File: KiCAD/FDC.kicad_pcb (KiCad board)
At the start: 2 copper layers, 72.6 x 65.5 mm, 26 parts, among them J2 Conn_02x20_Odd_Even, J3 SD_Card, Q1 SSM3K324RLFCT-ND, Q2 SSM3K324RLFCT-ND, U1 SN74LVCC4245ADWR, U2 Pico, U3 SN74LVCC4245ADWR, U4 SN74LVCC4245ADWR, U5 SN74LVCC4245ADWR

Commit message: First upload of test board.
First upload of test board.
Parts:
- removed the C4 at (182.7, 80.7)
- removed C5, C6, C7, C8: 100nF, Capacitor_SMD:C_0805_2012Metric_Pad1.18x1.45mm_HandSolder
- removed D2: PMEG4010CEJ, Diode_SMD:D_SOD-323F
- removed J2: Conn_02x20_Odd_Even, Connector_PinSocket_2.54mm:PinSocket_2x20_P2.54mm_Vertical
- removed J3: SD_Card, Connector_Card:SD_Kyocera_145638009511859+
- removed the R2 at (137.7, 79.6)
- removed U4, U5: SN74LVCC4245ADWR, Package_SO:SOIC-24W_7.5x15.4mm_P1.27mm
- added J1: Conn_01x04, Connector_PinHeader_2.54mm:PinHeader_1x04_P2.54mm_Vertical, F.Cu at (142.3, 70.7)
- added R1: 1k, Resistor_SMD:R_0805_2012Metric_Pad1.20x1.40mm_HandSolder, F.Cu at (137.5, 49.0)
- added SDCARD1: ST-TF-003A, 00-ProjectLib:MicroSD_Card_TB, F.Cu at (145.7, 38.8)
- added U2: 74HCT245, Package_SO:SOIC-20W_7.5x15.4mm_P1.27mm, F.Cu at (143.1, 107.0)
- added U6: Z80, Package_DIP:DIP-40_W15.24mm, F.Cu at (116.5, 87.9)
- added U7: Z80, Package_DIP:DIP-40_W15.24mm, F.Cu at (113.0, 87.9)
- C4: renamed from C9; moved to F.Cu
- D1: footprint LED_SMD:LED_2816_7142Metric_Pad3.20x4.45mm_HandSolder -> LED_THT:LED_D5.0mm
- PICO2: renamed from U2; value Pico -> Pico 2; footprint MCU_RaspberryPi_and_Boards:RPi_Pico_SMD_TH -> Module:RaspberryPi_Pico_SMD
- Q1, Q2: value SSM3K324RLFCT-ND -> 2N7002
- R2: renamed from R3; moved to F.Cu
- R3: renamed from R4; moved to F.Cu
- U1, U3: value SN74LVCC4245ADWR -> 74HCT245; footprint Package_SO:SOIC-24W_7.5x15.4mm_P1.27mm -> Package_SO:SOIC-20W_7.5x15.4mm_P1.27mm
- moved R5 83.7 mm to (122.0, 121.5), turned to 0 degrees
- moved Q2 82.9 mm to (122.5, 118.3), turned to 180 degrees
- moved D1 69.9 mm to (144.0, 51.0)
- moved R4 69.9 mm to (123.8, 128.5), turned to 180 degrees
- moved Q1 66.3 mm to (123.0, 125.5), turned to 0 degrees
- moved R6 63.1 mm to (140.8, 52.0)
- moved U1 56.4 mm to (143.1, 127.0), turned to 0 degrees
- moved C3 53.3 mm to (150.6, 117.5), turned to 0 degrees
- moved R3 52.5 mm to (143.0, 42.5), turned to -90 degrees
- moved R2 48.4 mm to (152.0, 42.5), turned to 90 degrees
- moved C4 47.3 mm to (147.0, 42.5), turned to -90 degrees
- moved PICO2 47.3 mm to (123.2, 50.0), turned to 0 degrees
- moved C2 29.9 mm to (151.1, 97.5), turned to 0 degrees
- moved C1 15.7 mm to (150.6, 77.0), turned to 0 degrees
- moved U3 14.7 mm to (143.0, 86.5), turned to 0 degrees
- renumbered R6 to R4, R8 to R5, R1 to R6
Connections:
- C1 pad 1: +3V3 -> +5V
- C2 pad 1: +3V3 -> +5V
- PICO2 pad 15: /RD' -> /RD*
- PICO2 pad 16: /WR' -> /WR*
- R2 pad 1: Net-(J3-DAT1) -> +3V3
- R2 pad 2: +3V3 -> Net-(SDCARD1-DAT1)
- U1 pad 1: +5V -> /DIR
- U1 pad 10: /IN* -> GND
- U1 pad 11: GND -> /D4'
- U1 pad 12: GND -> /D7'
- U1 pad 13: GND -> /D1'
- U1 pad 14: /IN' -> /D6'
- U1 pad 15: /RD' -> /D3'
- U1 pad 16: /WR' -> /D5'
- U1 pad 17: /OUT' -> /D0'
- U1 pad 18: /MREQ' -> /D2'
- U1 pad 19: unconnected-(U1-B3-Pad19) -> /DATAB_OE
- U1 pad 2: +5V -> /D2
- U1 pad 20: unconnected-(U1-B2-Pad20) -> +5V
- U1 pad 3: /SYSRES* -> /D0
- U1 pad 4: unconnected-(U1-A2-Pad4) -> /D5
- U1 pad 5: unconnected-(U1-A3-Pad5) -> /D3
- U1 pad 6: /RAS* -> /D6
- U1 pad 7: /OUT* -> /D1
- U1 pad 8: /WR* -> /D7
- U1 pad 9: /RD* -> /D4
- U3 pad 10: /D2 -> GND
- U3 pad 11: GND -> /D0'
- U3 pad 12: GND -> /D1'
- U3 pad 13: GND -> /D2'
- U3 pad 14: /D2' -> /D3'
- U3 pad 15: /D0' -> /D7'
- U3 pad 16: /D5' -> /D6'
- U3 pad 17: /D3' -> /D5'
- U3 pad 18: /D6' -> /D4'
- U3 pad 19: /D1' -> /ADDRH_OE
- U3 pad 2: /DIR -> /A12
- U3 pad 20: /D7' -> +5V
- U3 pad 3: /D4 -> /A13
- U3 pad 4: /D7 -> /A14
- U3 pad 5: /D1 -> /A15
- U3 pad 6: /D6 -> /A11
- U3 pad 7: /D3 -> /A10
- U3 pad 8: /D5 -> /A9
- U3 pad 9: /D0 -> /A8
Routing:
- net GND: track 446.6 -> 40.2 mm, vias 6 -> 388
- net +3V3: track 199.1 -> 35.8 mm, vias 10 -> 0
- net /RD*: track 5.17 -> 96.1 mm, vias 0 -> 1
- net /WR*: track 4.64 -> 92.3 mm, vias 0 -> 1
- net /DATAB_OE: track 28.3 -> 109.0 mm, vias 0 -> 2
- net +5V: track 122.9 -> 197.1 mm, vias 9 -> 3
- net /DIR: track 22.7 -> 87.8 mm
- net /WAIT': track 44.5 -> 100.5 mm
- net /D4: track 12.1 -> 54.2 mm, vias 0 -> 1
- net /ADDRL_OE: track 33.4 -> 73.1 mm, vias 0 -> 4
- net /D6: track 10.6 -> 45.7 mm, vias 1 -> 0
- net /D3: track 11.0 -> 45.9 mm, vias 0 -> 1
- net /A11: track 16.4 -> 50.1 mm, vias 0 -> 1
- net /D5: track 10.5 -> 40.7 mm, vias 0 -> 1
- net /D7: track 11.6 -> 41.7 mm, vias 0 -> 1
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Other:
- board size 72.6 x 65.5 mm -> 47 x 115.5 mm
- board text added: "IN"
- board text added: "OUT"
- board text added: "Pico2"
- board text added: "Q1,Q2 - 2N7002 R1,R2,R3,R4,R5 - 1k C1,C2,C3,C4 - 100NF R6 - 100 OHM U1,U2,U3 - 74HCT245"
- board text added: "RAS"
- board text added: "SYSRES"
- board text added: "Z80"

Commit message: New PCB.. this may fit
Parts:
- PICO2: moved to B.Cu
- moved Q1 79.2 mm to (144.7, 49.4), turned to 180 degrees
- moved Q2 79.0 mm to (144.8, 42.5)
- moved R5 78.2 mm to (142.3, 46.0), turned to 180 degrees
- moved R4 78.1 mm to (142.3, 52.7)
- moved SDCARD1 32.1 mm to (163.7, 65.3), turned to -90 degrees
- moved R2 24.3 mm to (158.0, 66.0), turned to 0 degrees
- moved PICO2 22.8 mm to (140.3, 65.0), turned to 180 degrees
- moved C4 22.7 mm to (158.0, 62.3), turned to 180 degrees
- moved R3 22.2 mm to (158.0, 58.8), turned to 180 degrees
- moved U6 18.5 mm to (132.3, 97.5)
- moved U7 18.5 mm to (128.8, 97.5)
- moved D1 17.6 mm to (161.4, 48.4), turned to 180 degrees
- moved R1 15.4 mm to (134.3, 64.0)
- moved R6 13.9 mm to (154.6, 52.5), turned to -90 degrees
- moved U1 13.8 mm to (156.3, 131.1)
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- renumbered C3 to C1, C1 to C3
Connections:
- J1 pad 1: /IN' -> /SYSRES'
- J1 pad 2: /OUT' -> /IN'
- J1 pad 3: /MREQ' -> /OUT'
- J1 pad 4: /SYSRES' -> /MREQ'
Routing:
- net /WAIT*: track 10.1 -> 109.6 mm
- net /WAIT': track 100.5 -> 8.54 mm, vias 0 -> 1
- net /INT': track 97.9 -> 8.64 mm, vias 0 -> 1
- net /INT*: track 20.4 -> 105.2 mm, vias 2 -> 0
- net /DIR: track 87.8 -> 128.6 mm, vias 0 -> 3
- net /DATAB_OE: track 109.0 -> 70.1 mm, vias 2 -> 1
- net /D4': track 88.8 -> 126.0 mm, vias 5 -> 4
- net /ADDRH_OE: track 56.1 -> 19.3 mm, vias 2 -> 1
- net /OUT': track 41.0 -> 8.38 mm, vias 1 -> 0
- net /D1': track 72.9 -> 102.2 mm
- net /IN': track 34.1 -> 6.18 mm, vias 1 -> 0
- net /MREQ': track 38.8 -> 10.9 mm, vias 2 -> 0
- net /D6': track 95.5 -> 122.4 mm
- net /ADDRL_OE: track 73.1 -> 47.4 mm, vias 4 -> 1
- net /A8: track 11.1 -> 36.8 mm
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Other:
- board size 47 x 115.5 mm -> 53.5 x 110.5 mm
- board text added: "74HCT245"
- board text added: "<--Pin1"
- board text added: "Floppy80-M1 Internal version by dabone 2026 https://github.com/dabonetn/Floppy80-M1-Internal"
- board text added: "Socket-> Pins<-"
- board text removed: "Pico2"

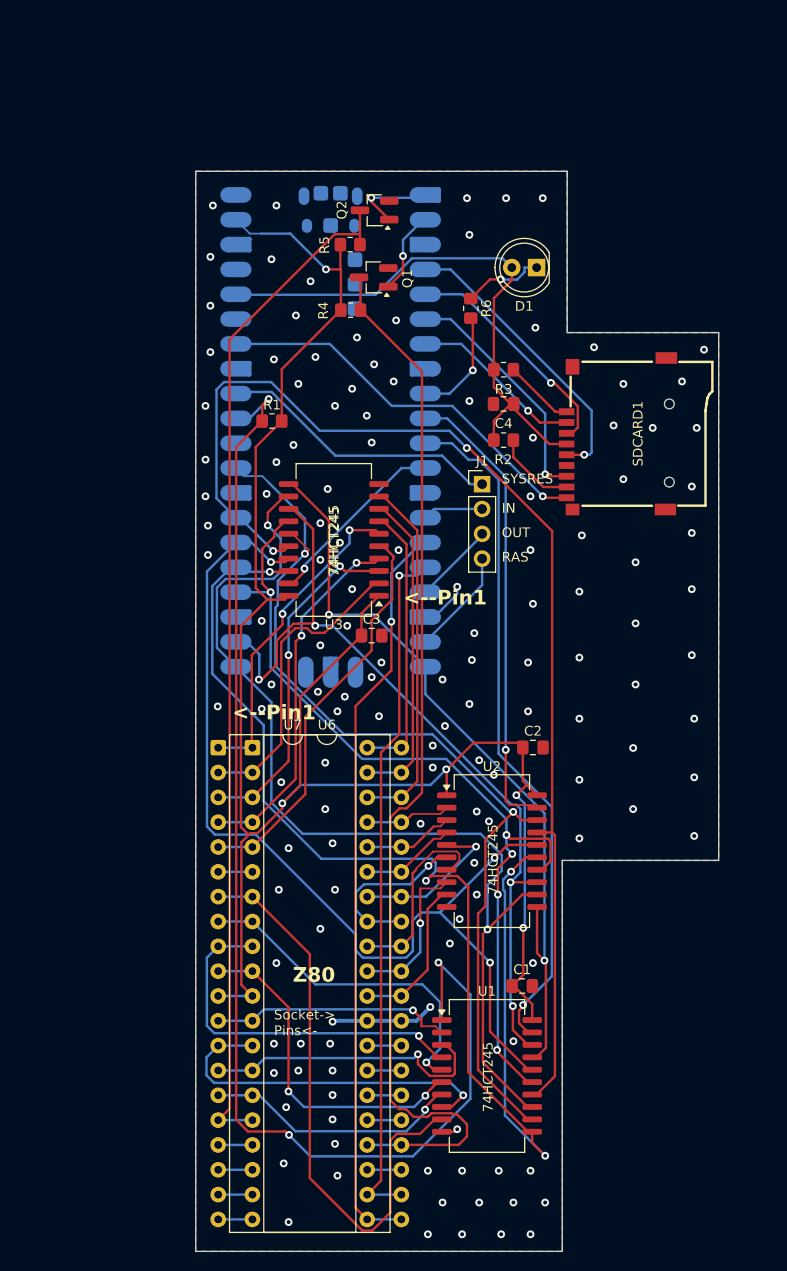
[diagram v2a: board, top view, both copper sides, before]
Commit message: Updated PCB to ver 1.01
I didn't account for some signals on the first pcb.
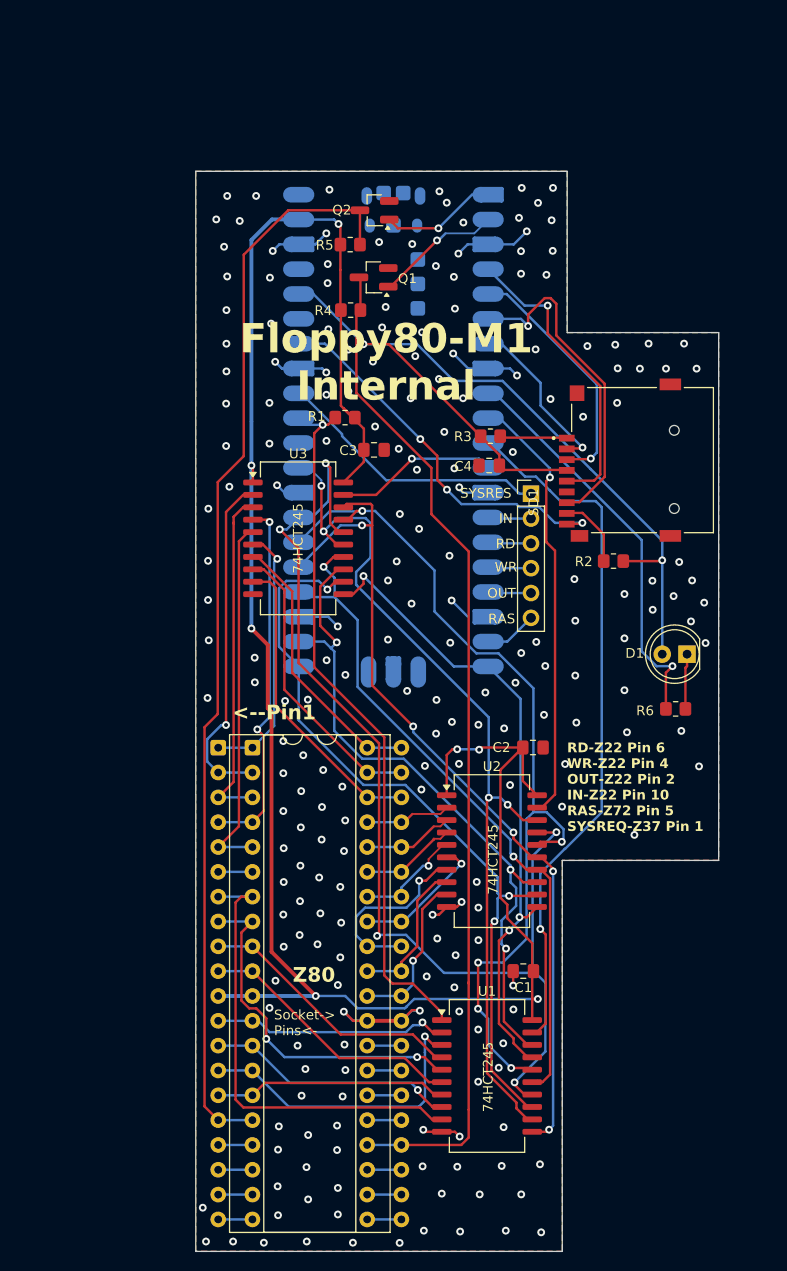
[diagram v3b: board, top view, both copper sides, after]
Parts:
- removed SDCARD1: ST-TF-003A, 00-ProjectLib:MicroSD_Card_TB
- added SD1: MSD-1-A, SDCard:CUI_MSD-1-A, F.Cu at (172.2, 68.0)
- J1: value Conn_01x04 -> Other Signals; footprint Connector_PinHeader_2.54mm:PinHeader_1x04_P2.54mm_Vertical -> Connector_PinHeader_2.54mm:PinHeader_1x06_P2.54mm_Vertical
- Q1, Q2: value 2N7002 -> FDV301N
- moved R6 46.0 mm to (175.6, 93.5), turned to 180 degrees
- moved D1 42.4 mm to (176.8, 87.9)
- moved C3 19.0 mm to (144.7, 67.0)
- moved R2 16.7 mm to (169.2, 78.4), turned to 180 degrees
- moved R1 7.48 mm to (141.8, 63.7)
- moved R3 6.93 mm to (156.7, 65.6)
- moved C4 6.47 mm to (156.5, 68.6)
- moved PICO2 6.43 mm to (146.7, 65.0)
- moved J1 5.09 mm to (160.8, 71.5)
- moved U3 3.65 mm to (137.0, 76.0), turned to 0 degrees
- moved C1 1.53 mm to (160.0, 120.3), turned to 180 degrees
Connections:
- J1 pad 3: /OUT' -> /RD'
- J1 pad 4: /MREQ' -> /WR'
- PICO2 pad 15: /RD* -> /RD'
- PICO2 pad 16: /WR* -> /WR'
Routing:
- net /RD*: track 76.4 -> 3.50 mm, vias 1 -> 0
- net /WR*: track 71.2 -> 3.50 mm, vias 1 -> 0
- net /DIR: track 128.6 -> 72.2 mm, vias 3 -> 1
- net GND: track 17.3 -> 62.6 mm, vias 139 -> 219
- net /D4': track 126.0 -> 87.3 mm, vias 4 -> 5
- net +3V3: track 58.2 -> 89.9 mm, vias 0 -> 2
- net /LED: track 11.3 -> 41.7 mm
- net /D1': track 102.2 -> 78.7 mm, vias 2 -> 3
- net /D3': track 88.9 -> 71.1 mm, vias 5 -> 2
- net /D2': track 85.5 -> 70.5 mm, vias 4 -> 3
- net /D0': track 79.1 -> 66.1 mm, vias 2 -> 3
- net /D5': track 103.8 -> 91.8 mm, vias 3 -> 5
- net /D4: track 59.5 -> 47.6 mm
- net /D7: track 36.8 -> 25.7 mm
- net +5V: track 194.1 -> 204.4 mm, vias 5 -> 7
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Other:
- board text added: "Floppy80-M1 Internal"
- board text added: "Floppy80-M1 ver 1.01 Internal version by dabone (2026) https://github.com/dabonetn/Floppy80-M1-Internal Original By MichaelM4 https://github.com/MichaelM4/Floppy80-M1"
- board text added: "Q1,Q2 - FDV301N R1,R2,R3,R4,R5 - 1k C1,C2,C3,C4 - 100NF R6 - 100 OHM U1,U2,U3 - 74HCT245"
- board text added: "RD"
- board text added: "RD-Z22 Pin 6 WR-Z22 Pin 4 OUT-Z22 Pin 2 IN-Z22 Pin 10 RAS-Z72 Pin 5 SYSREQ-Z37 Pin 1"
- board text added: "WR"
- board text removed: "Floppy80-M1 Internal version by dabone 2026 https://github.com/dabonetn/Floppy80-M1-Internal"
- board text removed: "Q1,Q2 - 2N7002 R1,R2,R3,R4,R5 - 1k C1,C2,C3,C4 - 100NF R6 - 100 OHM U1,U2,U3 - 74HCT245"

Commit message: New board revision
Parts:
- removed C1, C2, C3: 100nF, Capacitor_SMD:C_0805_2012Metric_Pad1.18x1.45mm_HandSolder
- removed the U1 at (156.3, 131.1)
- removed the U2 at (156.8, 108.0)
- added C23: 100nF, Capacitor_SMD:C_0805_2012Metric_Pad1.18x1.45mm_HandSolder, F.Cu at (158.4, 135.4)
- added C3-1: 100nF, Capacitor_SMD:C_0805_2012Metric_Pad1.18x1.45mm_HandSolder, F.Cu at (133.7, 92.3)
- added C3-2: 100nF, Capacitor_SMD:C_0805_2012Metric_Pad1.18x1.45mm_HandSolder, F.Cu at (133.5, 86.6)
- added C4: 100nF, Capacitor_SMD:C_0805_2012Metric_Pad1.18x1.45mm_HandSolder, F.Cu at (157.7, 119.1)
- added C5: 100nF, Capacitor_SMD:C_0805_2012Metric_Pad1.18x1.45mm_HandSolder, F.Cu at (137.4, 72.9)
- added C6: 100nF, Capacitor_SMD:C_0805_2012Metric_Pad1.18x1.45mm_HandSolder, F.Cu at (157.5, 99.0)
- added C7: 100nF, Capacitor_SMD:C_0805_2012Metric_Pad1.18x1.45mm_HandSolder, F.Cu at (146.7, 63.4)
- added U23: SN74LS32NSR, Package_SO:SOIC-14_3.9x8.7mm_P1.27mm, F.Cu at (154.6, 141.7)
- added U4: SN74LVC245APWR, Package_SO:TSSOP-20_4.4x6.5mm_P0.65mm, F.Cu at (154.8, 125.7)
- added U5: SN74LVC245APWR, Package_SO:TSSOP-20_4.4x6.5mm_P0.65mm, F.Cu at (140.4, 78.9)
- added U6: SN74LVC245APWR, Package_SO:TSSOP-20_4.4x6.5mm_P0.65mm, F.Cu at (154.8, 105.2)
- added U7: SN74LVC245APWR, Package_SO:TSSOP-20_4.4x6.5mm_P0.65mm, F.Cu at (143.6, 68.8)
- J1: value Other Signals -> Conn_01x01_Pin; footprint Connector_PinHeader_2.54mm:PinHeader_1x06_P2.54mm_Vertical -> Connector_PinHeader_2.54mm:PinHeader_1x01_P2.54mm_Vertical
- U3: value 74HCT245 -> SN74LVCC4245APWR; footprint Package_SO:SOIC-20W_7.5x15.4mm_P1.27mm -> Package_SO:TSSOP-24_4.4x7.8mm_P0.65mm
- moved J1 28.6 mm to (132.3, 74.1)
- moved U3 13.9 mm to (140.3, 89.5), turned to 90 degrees
- moved R6 11.3 mm to (176.9, 82.3), turned to 90 degrees
- moved R1 7.59 mm to (134.4, 61.9), turned to 90 degrees
- renumbered C4 to C-SD1, U7 to U1, U6 to U2
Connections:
- J1 pad 1: /SYSRES' -> /SYSRES*
- R1 pad 2: +5V -> +3V3
- U3 pad 10: GND -> /D4
- U3 pad 11: /D0' -> GND
- U3 pad 12: /D1' -> GND
- U3 pad 13: /D2' -> GND
- U3 pad 14: /D3' -> /D4-
- U3 pad 15: /D7' -> /D7-
- U3 pad 16: /D6' -> /D1-
- U3 pad 17: /D5' -> /D6-
- U3 pad 18: /D4' -> /D3-
- U3 pad 19: /ADDRH_OE -> /D5-
- U3 pad 2: /A12 -> /RD*
- U3 pad 20: +5V -> /D0-
- U3 pad 3: /A13 -> /D2
- U3 pad 4: /A14 -> /D0
- U3 pad 5: /A15 -> /D5
- U3 pad 6: /A11 -> /D3
- U3 pad 7: /A10 -> /D6
- U3 pad 8: /A9 -> /D1
- U3 pad 9: /A8 -> /D7
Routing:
- net +3V3: track 89.9 -> 231.4 mm, vias 2 -> 4
- net /MREQ: track 3.50 -> 118.4 mm, vias 0 -> 4
- net /IN5V: track 0.00 -> 114.0 mm, vias 0 -> 6
- net /OUT5V: track 0.00 -> 100.7 mm, vias 0 -> 4
- net /WR5V: track 0.00 -> 87.9 mm, vias 0 -> 6
- net /RD5V: track 0.00 -> 85.8 mm, vias 0 -> 2
- net /RD*: track 3.50 -> 79.5 mm
- net +5V: track 204.4 -> 147.5 mm, vias 7 -> 4
- net /A13: track 35.7 -> 87.6 mm, vias 0 -> 9
- net /DIR: track 72.2 -> 24.7 mm, vias 1 -> 2
- net /DATAB_OE: track 71.8 -> 27.5 mm, vias 1 -> 3
- net /D1': track 78.7 -> 120.7 mm, vias 3 -> 4
- net GND: track 62.6 -> 102.3 mm, vias 219 -> 147
- net /WAIT*: track 103.8 -> 135.2 mm, vias 0 -> 1
- net /IORQ: track 3.50 -> 34.1 mm, vias 0 -> 2
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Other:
- board text added: "1"
- board text added: "All Caps - 100NF R1,R2,R3,R4,R5 - 1k R6 - 100 OHM U3 - SN74LVCC4245APWR U4,U5,U6, U7 - SN74LVC245APWR U23 - SN74LS32NSR SD - MSD-1-A Q1,Q2 - FDV301N"
- board text added: "Floppy80-M1 ver 1.21 Internal version by dabone (2026) https://github.com/dabonetn/Floppy80-M1-Internal Original By MichaelM4 https://github.com/MichaelM4/Floppy80-M1"
- board text added: "SYSRES Via Near Pin 2"
- board text removed: "74HCT245"
- board text removed: "<--Pin1"
- board text removed: "Floppy80-M1 ver 1.01 Internal version by dabone (2026) https://github.com/dabonetn/Floppy80-M1-Internal Original By MichaelM4 https://github.com/MichaelM4/Floppy80-M1"
- board text removed: "IN"
- board text removed: "OUT"
- board text removed: "Q1,Q2 - FDV301N R1,R2,R3,R4,R5 - 1k C1,C2,C3,C4 - 100NF R6 - 100 OHM U1,U2,U3 - 74HCT245"
- board text removed: "RAS"
- board text removed: "RD"
- board text removed: "RD-Z22 Pin 6 WR-Z22 Pin 4 OUT-Z22 Pin 2 IN-Z22 Pin 10 RAS-Z72 Pin 5 SYSREQ-Z37 Pin 1"
- board text removed: "SYSRES"
- board text removed: "WR"
